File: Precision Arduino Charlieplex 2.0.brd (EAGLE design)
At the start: 76.2 x 76.2 mm, 272 parts, among them U401 ATMEGA328, U501 FT232RLSSOP, U602 ZF7, Y401 16MHz

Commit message: Merged Mio's KwanSystems.lbr, updated all eagle files to use it.
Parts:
- removed D200, D201, D202, D203, D204, D205, D206, D207, D208, D209, D210, D211, D212, D213, D214, D215, D216, D217, D218, D219, D220, D221, D222, D223, D224, D225, D226, D227, D228, D229, D230, D231, D232, D233, D234, D235, D236, D237, D238, D239, D240, D241, D242, D243, D244, D245, D246, D247, D248, D249, D250, D251, D252, D253, D254, D255, D256, D257, D258, D259: GREEN, SparkFun-LED:LED-0603
- removed D300, D301, D302, D303, D304, D305, D306, D307, D308, D309, D310, D311, D312, D313, D314, D315, D316, D317, D318, D319, D320, D321, D322, D323, D324, D325, D326, D327, D328, D329, D330, D331, D332, D333, D334, D335, D336, D337, D338, D339, D340, D341, D342, D343, D344, D345, D346, D347, D348, D349, D350, D351, D352, D353, D354, D355, D356, D357, D358, D359: BLUE, SparkFun-LED:LED-0603
- added D060, D061, D062: HOUR, SparkFun:LED-0603
- D000, D001, D002, D003, D004, D005, D006, D007, D008, D009, D010, D011, D012, D013, D014, D015, D016, D017, D018, D019, D020, D021, D022, D023, D024, D025, D026, D027, D028, D029, D030, D031, D032, D033, D034, D035, D036, D037, D038, D039, D040, D041, D042, D043, D044, D045, D046, D047, D048, D049, D050, D051, D052, D053, D054, D055, D056, D057, D058, D059: value RED -> HOUR; device SparkFun-LED:LED-0603 -> SparkFun:LED-0603
- D100, D101, D102, D103, D104, D105, D106, D107, D108, D109, D110, D111, D112, D113, D114, D115, D116, D117, D118, D119, D120, D121, D122, D123, D124, D125, D126, D127, D128, D129, D130, D131, D132, D133, D134, D135, D136, D137, D138, D139, D140, D141, D142, D143, D144, D145, D146, D147, D148, D149, D150, D151, D152, D153, D154, D155, D156, D157, D158, D159: value YELLOW -> HOUR; device SparkFun-LED:LED-0603 -> SparkFun:LED-0603
- S429: value B3U-1100P -> B3U-1000P; device KwanSystems:B3U-1100P -> KwanSystems:B3U-1000P
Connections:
- net GND: no longer S429.P$3, Y401.2, Y401.4
- net Q01: now also D060.A, D061.A
- net Q02: now also D062.A

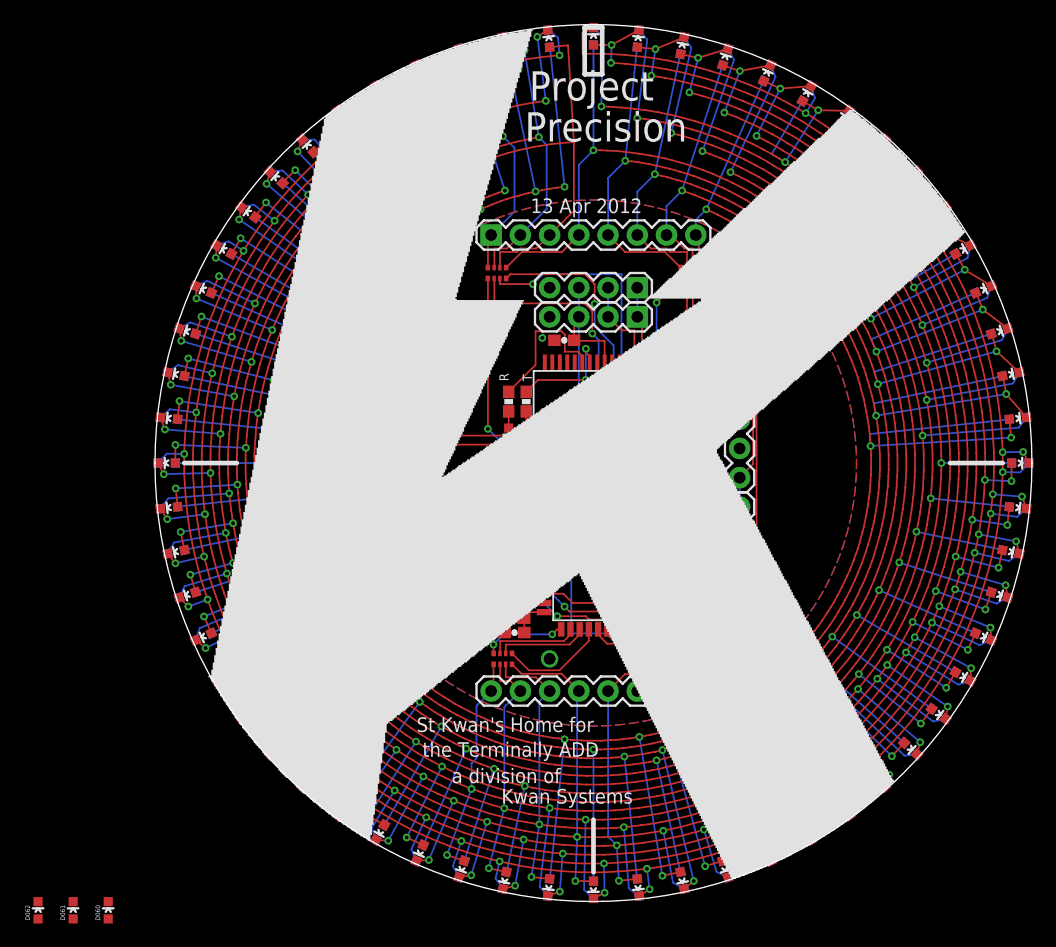
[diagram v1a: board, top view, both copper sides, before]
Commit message: Preparing for check against workspace~ and workspace2
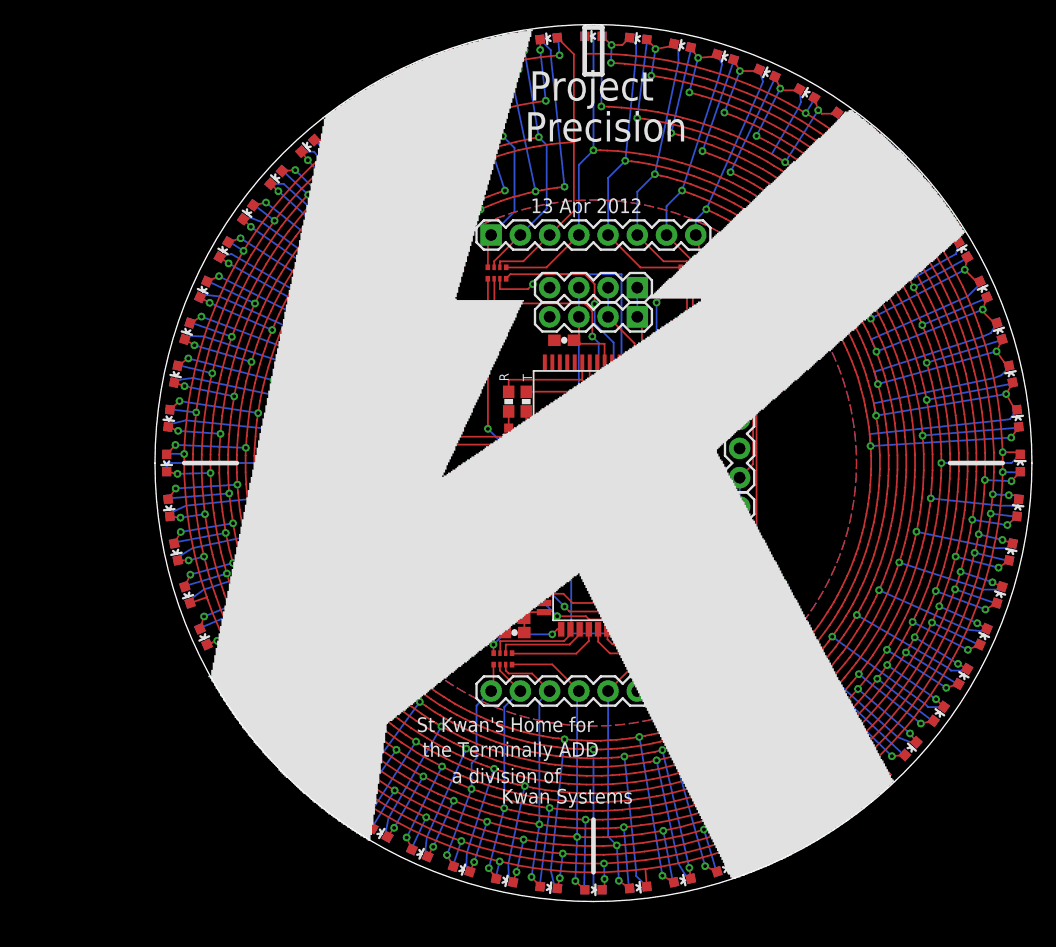
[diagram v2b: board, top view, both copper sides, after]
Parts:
- removed D060, D061, D062: HOUR, SparkFun:LED-0603
- turned D000 to 90 degrees
- turned D001 to 84 degrees
- turned D002 to 78 degrees
- turned D003 to 72 degrees
- turned D004 to 66 degrees
- turned D005 to 60 degrees
- turned D006 to 54 degrees
- turned D007 to 48 degrees
- turned D008 to 42 degrees
- turned D009 to 36 degrees
- turned D010 to 30 degrees
- turned D011 to 24 degrees
- turned D012 to 18 degrees
- turned D013 to 12 degrees
- turned D014 to 6 degrees
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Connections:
- net GND: now also Y401.2, Y401.4
- net Q01: no longer D060.A, D061.A
- net Q02: no longer D062.A
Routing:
- net Q01: track 282.8 -> 265.8 mm, vias 18 -> 11
- net Q02: track 281.3 -> 265.3 mm
- net Q03: track 278.6 -> 262.8 mm
- net Q04: track 281.7 -> 266.6 mm
- net Q05: track 286.7 -> 272.4 mm
- net Q06: track 290.8 -> 276.8 mm
- net Q11: track 315.3 -> 302.6 mm
- net Q07: track 296.1 -> 284.1 mm
- net Q08: track 297.9 -> 288.6 mm
- net Q16: track 336.5 -> 345.6 mm
- net Q12: track 311.1 -> 302.5 mm
- net Q13: track 306.6 -> 298.5 mm
- net GPS_TX: track 27.9 -> 20.7 mm
- net Q15: track 321.2 -> 328.1 mm
- net Q09: track 303.5 -> 296.7 mm
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
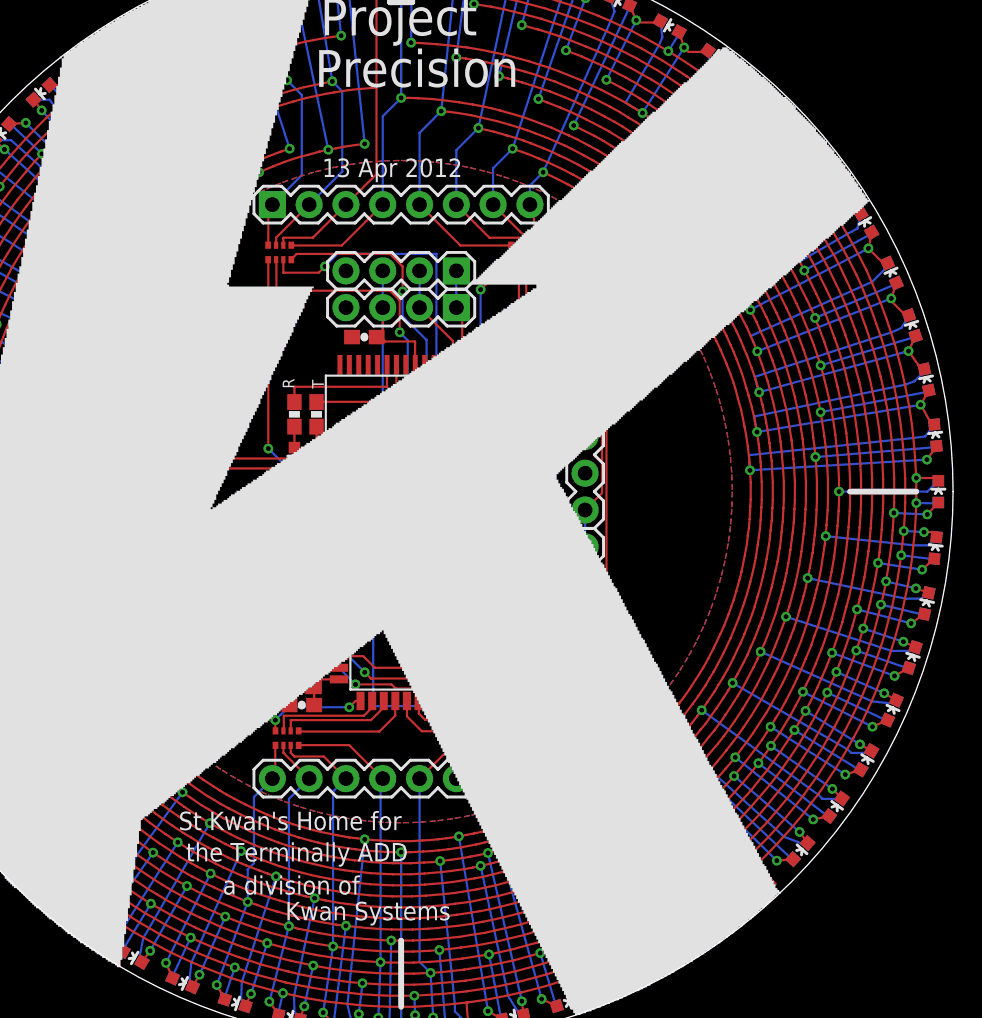
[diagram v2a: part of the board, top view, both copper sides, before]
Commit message: Started RocketometerATMega.sch, finished PrecisionATMega32U4
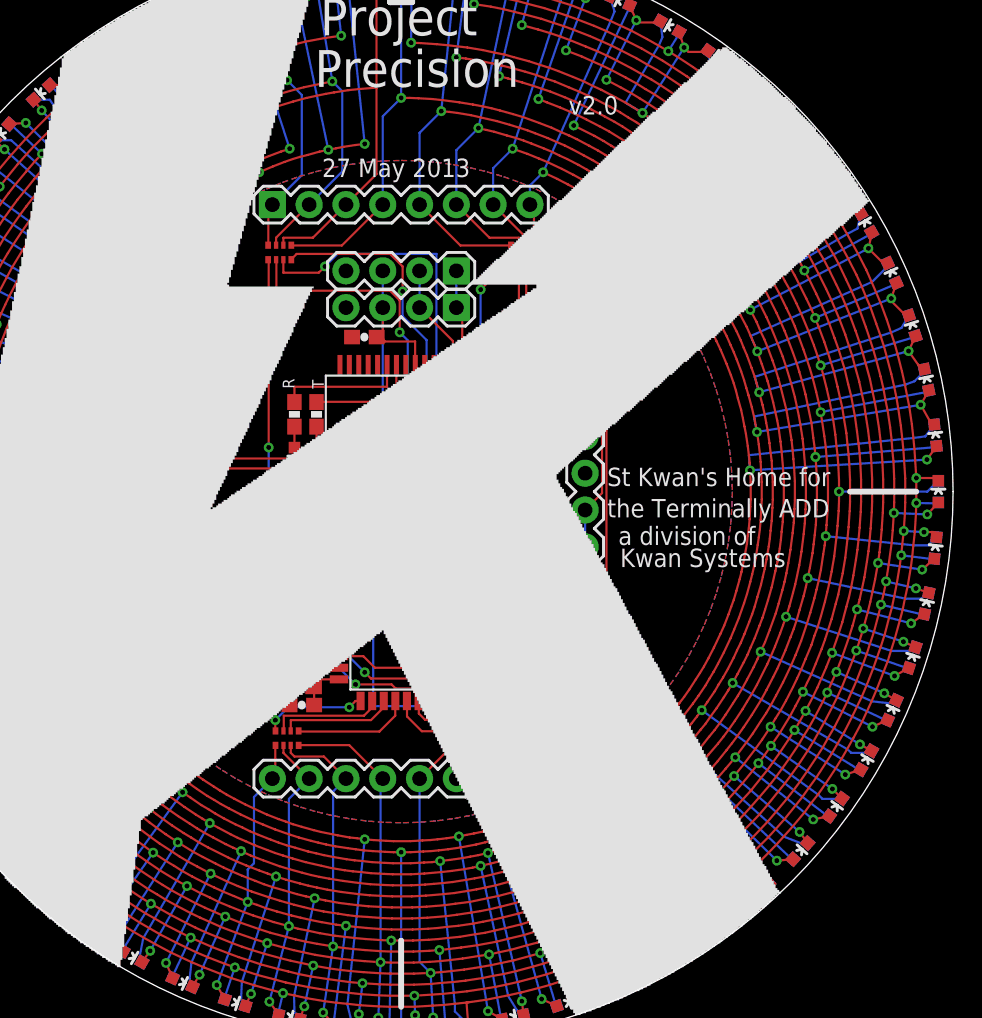
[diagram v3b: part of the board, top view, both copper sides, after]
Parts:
- removed J005: (no value), SparkFun:1X06
- removed JP5: (no value), SparkFun:1X02
- J004: device SparkFun:1X04 -> SparkFun:1X06
- moved J004 12.7 mm to (50.8, 31.8), turned to 90 degrees
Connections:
- net 3V3: now also J004.2, J004.3; no longer J004.4, JP5.1
- net AT_TX: now also J004.6; no longer J004.1
- net D12: no longer J005.5
- net GND: now also J004.4; no longer J004.3, J005.3
- net GPS_TX: now also J004.5; no longer J004.2
- net P01: no longer J005.6
- net P16: no longer J005.4
- net PPS: now also J004.1; no longer JP5.2
- net RESET: no longer J005.1
- net VCC: no longer J005.2
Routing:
- net RESET: track 46.3 -> 43.8 mm
- net P01: track 35.8 -> 33.3 mm
- net VCC: track 77.0 -> 74.5 mm
- net P16: track 72.8 -> 70.2 mm
- net P15: track 26.4 -> 28.6 mm
- net P09: track 25.6 -> 26.7 mm
- net P14: track 25.0 -> 25.9 mm
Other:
- board text added: "27 May 2013"
- board text added: "v2.0"
- board text removed: "13 Apr 2012"
